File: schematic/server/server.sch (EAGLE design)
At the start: 28 parts

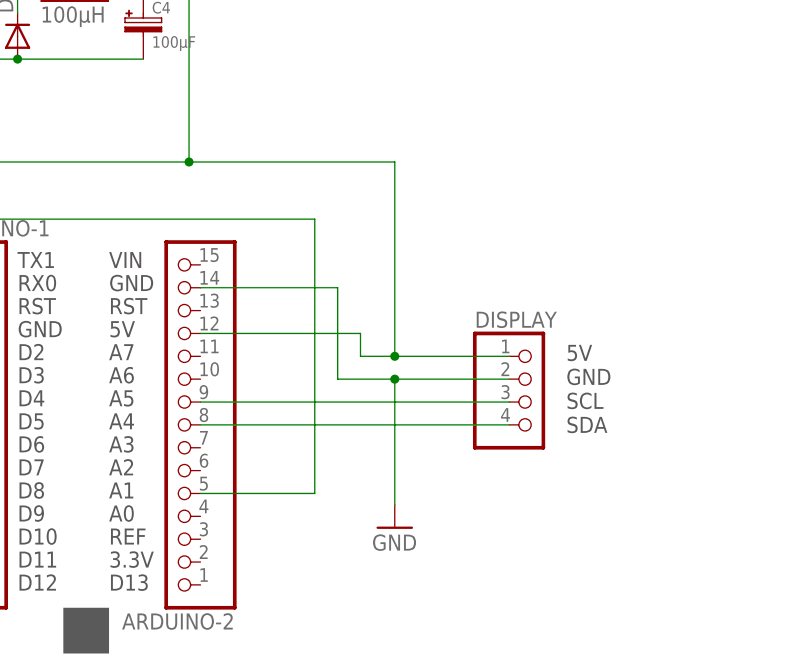
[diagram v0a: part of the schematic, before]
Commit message: pinoutChange
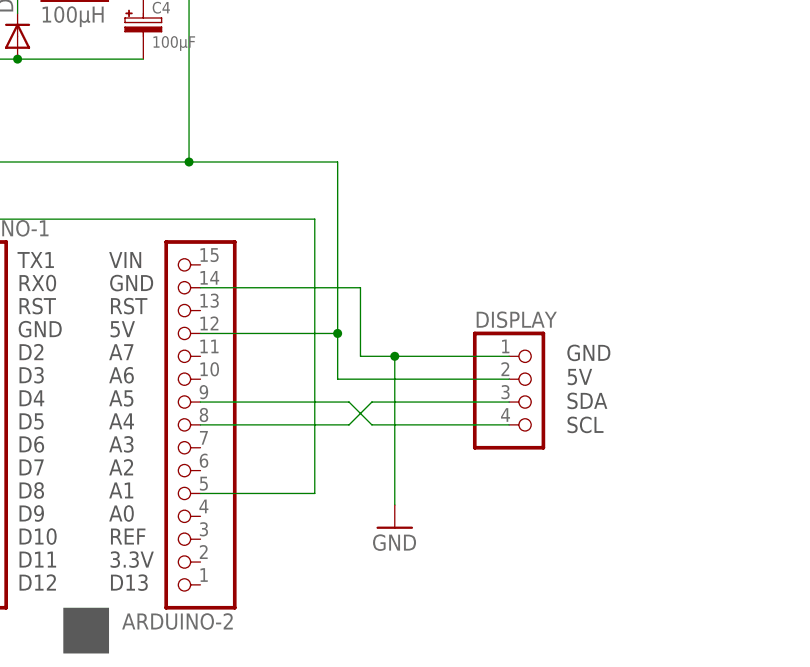
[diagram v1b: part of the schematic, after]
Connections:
- removed net N$20: ARDUINO-2.9, DISPLAY.3
- removed net N$21: ARDUINO-2.8, DISPLAY.4
- new net N$10: ARDUINO-2.9, DISPLAY.4
- new net N$8: ARDUINO-2.8, DISPLAY.3
- net GND: now also DISPLAY.1; no longer DISPLAY.2
- net N$18: now also DISPLAY.2; no longer DISPLAY.1
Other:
- note added: "GND 5V SDA SCL"
- note removed: "5V GND SCL SDA"
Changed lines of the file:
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@@
 <text x="13.97" y="157.48" size="1.778" layer="97">GND
 7-12V</text>
-<text x="231.14" y="105.41" size="1.778" layer="97" rot="MR180">5V
-GND
-SCL
-SDA</text>
+<text x="231.14" y="105.41" size="1.778" layer="97" rot="MR180">GND
+5V
+SDA
+SCL</text>
 <text x="180.34" y="78.105" size="1.778" layer="97" distance="44">VIN
 GND
@@
 </segment>
 </net>
-<net name="N$20" class="0">
-<segment>
-<pinref part="DISPLAY" gate="A" pin="3"/>
-<pinref part="ARDUINO-2" gate="A" pin="9"/>
-<wire x1="224.79" y1="99.06" x2="190.5" y2="99.06" width="0.1524" layer="91"/>
-</segment>
-</net>
-<net name="N$21" class="0">
-<segment>
-<pinref part="DISPLAY" gate="A" pin="4"/>
-<pinref part="ARDUINO-2" gate="A" pin="8"/>
-<wire x1="224.79" y1="96.52" x2="190.5" y2="96.52" width="0.1524" layer="91"/>
-</segment>
-</net>
 <net name="N$1" class="0">
 <segment>
@@
 </segment>
 <segment>
-<pinref part="DISPLAY" gate="A" pin="2"/>
-<wire x1="224.79" y1="101.6" x2="212.09" y2="101.6" width="0.1524" layer="91"/>
-<wire x1="212.09" y1="101.6" x2="205.74" y2="101.6" width="0.1524" layer="91"/>
-<wire x1="205.74" y1="101.6" x2="205.74" y2="111.76" width="0.1524" layer="91"/>
+<wire x1="212.09" y1="104.14" x2="208.28" y2="104.14" width="0.1524" layer="91"/>
+<wire x1="208.28" y1="104.14" x2="208.28" y2="111.76" width="0.1524" layer="91"/>
 <pinref part="ARDUINO-2" gate="A" pin="14"/>
-<wire x1="190.5" y1="111.76" x2="205.74" y2="111.76" width="0.1524" layer="91"/>
+<wire x1="190.5" y1="111.76" x2="208.28" y2="111.76" width="0.1524" layer="91"/>
 <pinref part="GND5" gate="1" pin="GND"/>
-<wire x1="212.09" y1="87.63" x2="212.09" y2="101.6" width="0.1524" layer="91"/>
-<junction x="212.09" y="101.6"/>
+<wire x1="212.09" y1="87.63" x2="212.09" y2="104.14" width="0.1524" layer="91"/>
+<junction x="212.09" y="104.14"/>
+<pinref part="DISPLAY" gate="A" pin="1"/>
+<wire x1="212.09" y1="104.14" x2="224.79" y2="104.14" width="0.1524" layer="91"/>
 </segment>
 </net>
@@
 <net name="N$18" class="0">
 <segment>
-<wire x1="212.09" y1="104.14" x2="208.28" y2="104.14" width="0.1524" layer="91"/>
-<wire x1="208.28" y1="104.14" x2="208.28" y2="106.68" width="0.1524" layer="91"/>
+<wire x1="205.74" y1="101.6" x2="205.74" y2="106.68" width="0.1524" layer="91"/>
 <pinref part="ARDUINO-2" gate="A" pin="12"/>
-<wire x1="190.5" y1="106.68" x2="208.28" y2="106.68" width="0.1524" layer="91"/>
-<junction x="212.09" y="104.14"/>
-<pinref part="DISPLAY" gate="A" pin="1"/>
-<wire x1="212.09" y1="104.14" x2="224.79" y2="104.14" width="0.1524" layer="91"/>
+<wire x1="190.5" y1="106.68" x2="205.74" y2="106.68" width="0.1524" layer="91"/>
 <pinref part="L2" gate="G$1" pin="2"/>
 <pinref part="C4" gate="G$1" pin="P$2"/>
@@
 <wire x1="97.79" y1="96.52" x2="91.44" y2="96.52" width="0.1524" layer="91"/>
 <wire x1="91.44" y1="125.73" x2="91.44" y2="96.52" width="0.1524" layer="91"/>
-<wire x1="212.09" y1="104.14" x2="212.09" y2="125.73" width="0.1524" layer="91"/>
-<wire x1="212.09" y1="125.73" x2="189.23" y2="125.73" width="0.1524" layer="91"/>
+<wire x1="205.74" y1="106.68" x2="205.74" y2="125.73" width="0.1524" layer="91"/>
+<wire x1="205.74" y1="125.73" x2="189.23" y2="125.73" width="0.1524" layer="91"/>
 <junction x="189.23" y="125.73"/>
-</segment>
-</net>
+<pinref part="DISPLAY" gate="A" pin="2"/>
+<wire x1="205.74" y1="101.6" x2="224.79" y2="101.6" width="0.1524" layer="91"/>
+<junction x="205.74" y="106.68"/>
+</segment>
+</net>
+<net name="N$8" class="0">
+<segment>
+<pinref part="DISPLAY" gate="A" pin="3"/>
+<wire x1="224.79" y1="99.06" x2="209.55" y2="99.06" width="0.1524" layer="91"/>
+<wire x1="209.55" y1="99.06" x2="207.01" y2="96.52" width="0.1524" layer="91"/>
+<pinref part="ARDUINO-2" gate="A" pin="8"/>
+<wire x1="207.01" y1="96.52" x2="190.5" y2="96.52" width="0.1524" layer="91"/>
+</segment>
+</net>
+<net name="N$10" class="0">
+<segment>
+<pinref part="ARDUINO-2" gate="A" pin="9"/>
+<wire x1="190.5" y1="99.06" x2="207.01" y2="99.06" width="0.1524" layer="91"/>
+<wire x1="207.01" y1="99.06" x2="209.55" y2="96.52" width="0.1524" layer="91"/>
+<pinref part="DISPLAY" gate="A" pin="4"/>
+<wire x1="209.55" y1="96.52" x2="224.79" y2="96.52" width="0.1524" layer="91"/>
+</segment>
+</net>
